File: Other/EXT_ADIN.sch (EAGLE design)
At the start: 19 parts, among them IC1 TINY45, Q1 IRLU3410, Q2 IRLU3410, Q3 IRLU3410, X2 PW1

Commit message: Added ...
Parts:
- removed IC1: TINY45, atmel:TINY15LS
- removed R1, R2, R3: 10k, RCL:R0603
- removed R4, R5, R6: 330R, RCL:R0603
- removed XS1: 1727049, Conn:1727049
- added C2, C3, C4, C5, C6: 33n, RCL:C1206
- added LED4, LED5, LED6: YELLOW, Optic:LED1206
- added Q4, Q5, Q6: BSS139, Transistor:FET-ND23
- added R1.1, R1.2: 3k3, RCL:R1206
- added R1.3, R1.4, R1.5, R1.6: 39k, RCL:R1206
- added R2.1, R2.2: 6k8, RCL:R1206
- added R2.3, R2.4, R2.5, R2.6: 10k, RCL:R1206
- added R26, R27, R28, R29, R30, R31: 470R, RCL:R1206
- added R3.1, R3.5, R3.6, R4.1, R4.2, R4.3, R4.4: n.b., RCL:R1206
- added R3.2: 560R, RCL:R1206
- added R3.3, R3.4, R4.5, R4.6: 3k6, RCL:R1206
- added XS2: 1727078, Conn:CON8-SS381
- added ZD1, ZD2, ZD3, ZD4, ZD5, ZD6: (no value), Diode:ZDSOD80
- C1: value 1u -> 33n; device RCL:C0603 -> RCL:C1206
- LED1: value LEDR -> GREEN
- LED2: value LEDG -> GREEN
- LED3: value LEDB -> YELLOW
- Q1, Q2, Q3: value IRLU3410 -> BSS139; device Transistor:FET-ND251 -> Transistor:FET-ND23
- X2: value PW1 -> (none)
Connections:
- removed net +3V3: C1.2, IC1.VCC, IN-11.S, OUT-11.S, R1.1, R2.1, R3.1
- removed net BLUE: IC1.(ADC2)PB3, Q3.G, R6.2
- removed net GREEN: IC1.(OCP)PB1, Q2.G, R5.2
- removed net N$7: Q2.D, XS1-3.K
- removed net RED: IC1.(ADC3)PB4, Q1.G, R4.2
- removed net RST: IC1.(ADC0)PB5, R1.2
- new net 3V3: IN-11.S, OUT-11.S
- new net AI6: C1.1, IN-20.S, Q1.G, R1.1.1, R2.1.1, ZD1.C
- new net AI7: C2.1, IN-19.S, Q2.G, R1.2.1, R2.2.1, ZD2.C
- new net N$10: LED2.A, R27.1
- new net N$11: Q2.S, R27.2
- new net N$12: LED3.A, R28.1
- new net N$13: Q3.S, R28.2
- new net N$14: LED4.A, R29.1
- new net N$15: Q4.S, R29.2
- new net N$16: LED5.A, R30.1
- new net N$17: Q5.S, R30.2
- new net N$18: LED6.A, R31.1
- new net N$19: Q6.S, R31.2
- new net N$2: R2.3.2, R3.3.2, R4.3.1, XS2-4.K
- new net VCC: Q1.D, Q2.D, Q3.D, Q4.D, Q5.D, Q6.D, R4.1.2, R4.2.2, R4.3.2, R4.4.2, R4.5.2, R4.6.2, X2.S, XS2-8.K
- net GND: now also C1.2, C2.2, C3.2, C4.2, C5.2, C6.2, LED4.C, LED5.C, LED6.C, R1.1.2, R1.2.2, R1.3.2, R1.4.2, R1.5.2, R1.6.2, R3.1.1, R3.2.1, R3.3.1, R3.4.1, R3.5.1, R3.6.1, XS2-3.K, ZD1.A, ZD2.A, ZD3.A, ZD4.A, ZD5.A, ZD6.A; no longer C1.1, IC1.GND, Q1.S, Q2.S, Q3.S, XS1-1.K
- net N$1: now also R2.2.2, R3.2.2, R4.2.1, XS2-2.K; no longer IN-20.S, OUT-20.S
- net N$3: now also R2.1.2, R3.1.2, R4.1.1, XS2-1.K; no longer IN-19.S, OUT-19.S
- net N$4: now also R2.4.2, R3.4.2, R4.4.1, XS2-5.K; no longer LED1.A, R4.1
- net N$5: now also R2.5.2, R3.5.2, R4.5.1, XS2-6.K; no longer LED2.A, R5.1
- net N$6: now also R2.6.2, R3.6.2, R4.6.1, XS2-7.K; no longer Q1.D, XS1-2.K
- net N$8: now also LED1.A, R26.1; no longer Q3.D, XS1-4.K
- net N$9: now also Q1.S, R26.2; no longer LED3.A, R6.1
- net PC0: now also C3.1, Q3.G, R1.3.1, R2.3.1, ZD3.C; no longer OUT-18.S
- net PC1: now also C4.1, Q4.G, R1.4.1, R2.4.1, ZD4.C; no longer OUT-17.S
- net PC2: now also C5.1, Q5.G, R1.5.1, R2.5.1, ZD5.C; no longer OUT-16.S
- net PC3: now also C6.1, Q6.G, R1.6.1, R2.6.1, ZD6.C; no longer OUT-15.S
- net PC4/SDA: no longer IC1.(AREF)PB0, R3.2
- net PC5/SCL: no longer IC1.(ADC1)PB2, R2.2
- net PD0: now also OUT-18.S; no longer OUT-10.S
- net PD1: now also OUT-17.S; no longer OUT-9.S
- net PD2: now also OUT-16.S; no longer OUT-8.S
- net PD3: now also OUT-15.S; no longer OUT-7.S
- net PD4: now also OUT-10.S; no longer OUT-6.S
- net PD5: now also OUT-9.S; no longer OUT-5.S
- net PD6: now also OUT-8.S; no longer OUT-4.S
- net PD7: now also OUT-7.S; no longer OUT-3.S
- net VIN: no longer X2.S, XS1-5.K
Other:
- note added: "0-10V"
- note added: "0-20mA"
- note added: "NPN"
- note added: "PNP"
- moved on the sheet: C1, IN-1, IN-10, IN-11, IN-12, IN-13, IN-14, IN-15, IN-16, IN-17, IN-18, IN-19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

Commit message: Reorganization
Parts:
- renumbered ZD1 to D1, ZD2 to D2, ZD3 to D3, ZD4 to D4, ZD5 to D5, ZD6 to D6

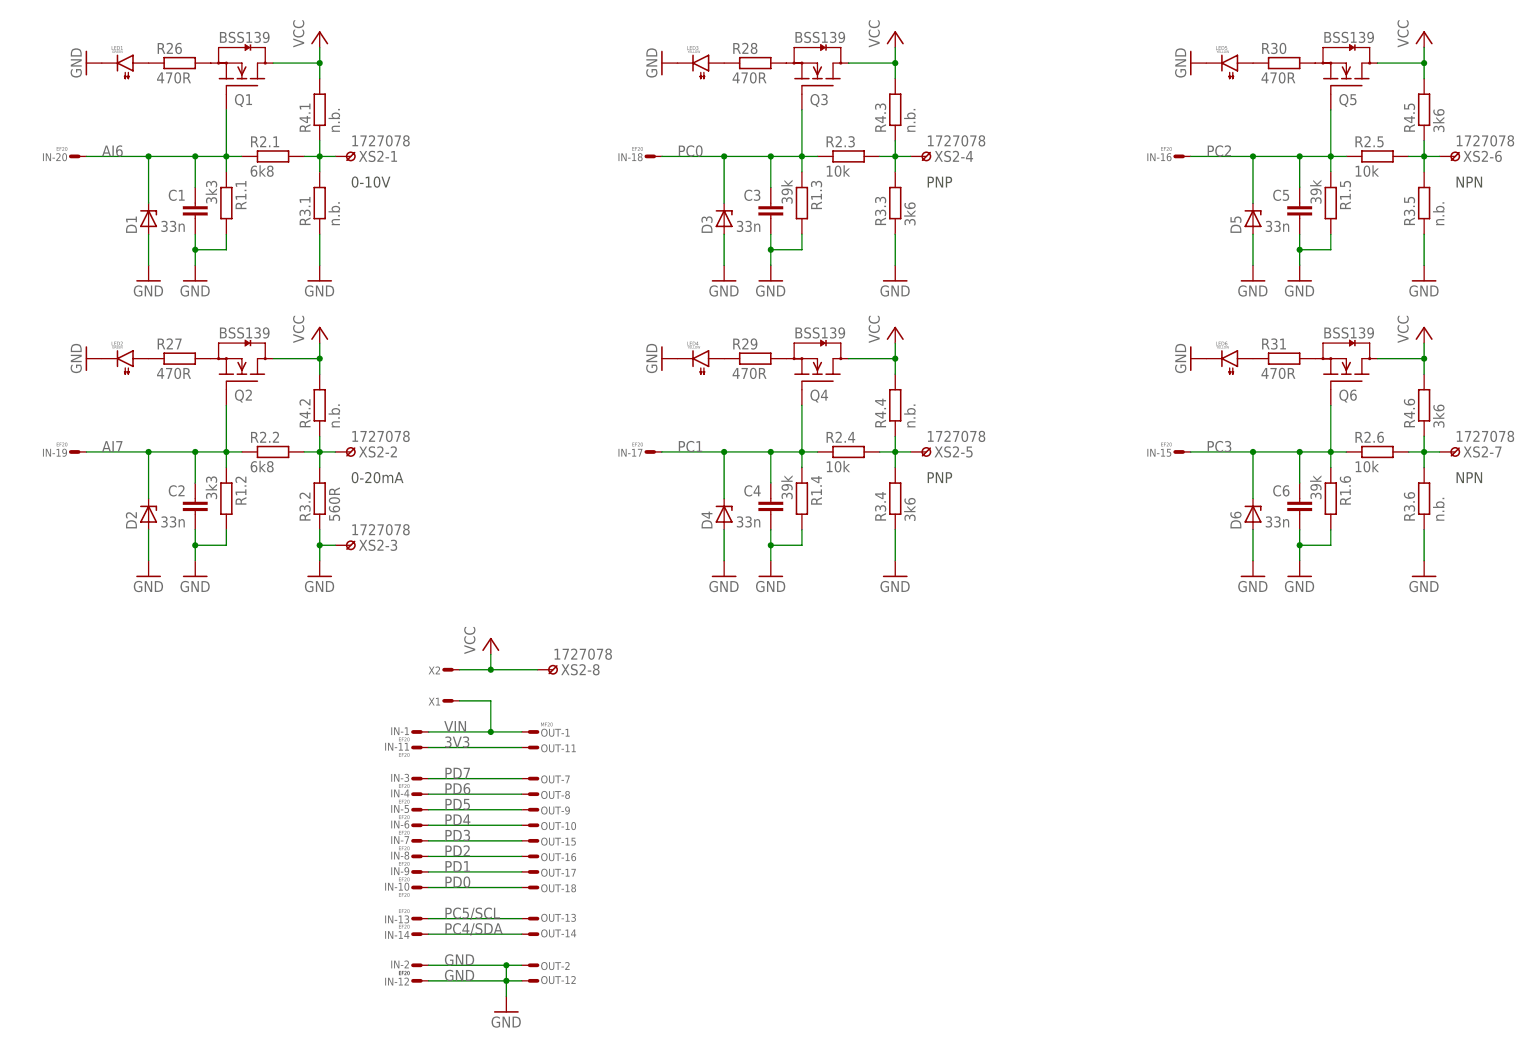
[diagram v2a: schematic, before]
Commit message: Optimized R
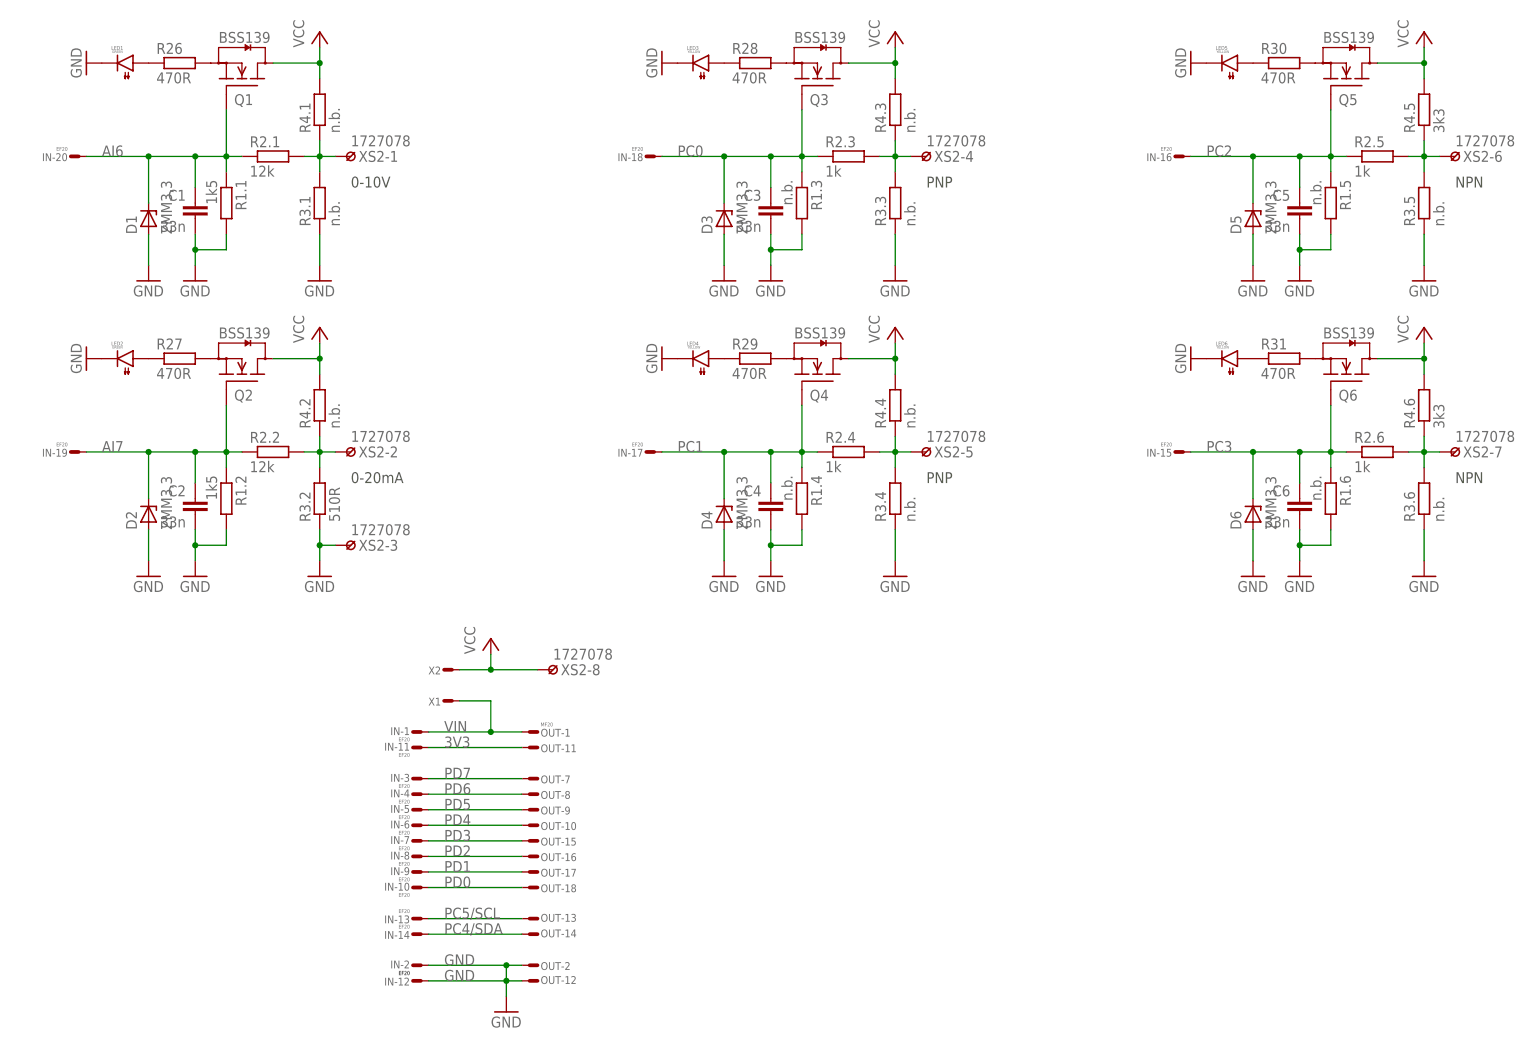
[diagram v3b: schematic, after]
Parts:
- D1, D2, D3, D4, D5, D6: value (none) -> ZMM3,3
- R1.1, R1.2: value 3k3 -> 1k5
- R1.3, R1.4, R1.5, R1.6: value 39k -> n.b.
- R2.1, R2.2: value 6k8 -> 12k
- R2.3, R2.4, R2.5, R2.6: value 10k -> 1k
- R3.2: value 560R -> 510R
- R3.3, R3.4: value 3k6 -> n.b.
- R4.5, R4.6: value 3k6 -> 3k3
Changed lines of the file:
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@@
 <part name="OUT" library="Conn" deviceset="ML20?E" device="LS" value="MF20"/>
 <part name="IN" library="Conn" deviceset="FE20E" device="LSS" value="EF20"/>
-<part name="R1.1" library="RCL" deviceset="R" device="1206" value="3k3"/>
-<part name="R2.1" library="RCL" deviceset="R" device="1206" value="6k8"/>
+<part name="R1.1" library="RCL" deviceset="R" device="1206" value="1k5"/>
+<part name="R2.1" library="RCL" deviceset="R" device="1206" value="12k"/>
 <part name="R3.1" library="RCL" deviceset="R" device="1206" value="n.b."/>
 <part name="GND1" library="supply1" deviceset="GND" device=""/>
@@
 <part name="GND2" library="supply1" deviceset="GND" device=""/>
 <part name="GND3" library="supply1" deviceset="GND" device=""/>
-<part name="D1" library="Diode" deviceset="ZD" device="SOD80"/>
+<part name="D1" library="Diode" deviceset="ZD" device="SOD80" value="ZMM3,3"/>
 <part name="GND4" library="supply1" deviceset="GND" device=""/>
 <part name="R4.1" library="RCL" deviceset="R" device="1206" value="n.b."/>
-<part name="R1.2" library="RCL" deviceset="R" device="1206" value="3k3"/>
-<part name="R2.2" library="RCL" deviceset="R" device="1206" value="6k8"/>
-<part name="R3.2" library="RCL" deviceset="R" device="1206" value="560R"/>
+<part name="R1.2" library="RCL" deviceset="R" device="1206" value="1k5"/>
+<part name="R2.2" library="RCL" deviceset="R" device="1206" value="12k"/>
+<part name="R3.2" library="RCL" deviceset="R" device="1206" value="510R"/>
 <part name="C2" library="RCL" deviceset="C" device="1206" value="33n"/>
 <part name="GND5" library="supply1" deviceset="GND" device=""/>
 <part name="GND6" library="supply1" deviceset="GND" device=""/>
-<part name="D2" library="Diode" deviceset="ZD" device="SOD80"/>
+<part name="D2" library="Diode" deviceset="ZD" device="SOD80" value="ZMM3,3"/>
 <part name="GND7" library="supply1" deviceset="GND" device=""/>
 <part name="R4.2" library="RCL" deviceset="R" device="1206" value="n.b."/>
 <part name="P+1" library="supply1" deviceset="VCC" device=""/>
 <part name="P+2" library="supply1" deviceset="VCC" device=""/>
-<part name="R1.3" library="RCL" deviceset="R" device="1206" value="39k"/>
-<part name="R2.3" library="RCL" deviceset="R" device="1206" value="10k"/>
-<part name="R3.3" library="RCL" deviceset="R" device="1206" value="3k6"/>
+<part name="R1.3" library="RCL" deviceset="R" device="1206" value="n.b."/>
+<part name="R2.3" library="RCL" deviceset="R" device="1206" value="1k"/>
+<part name="R3.3" library="RCL" deviceset="R" device="1206" value="n.b."/>
 <part name="C3" library="RCL" deviceset="C" device="1206" value="33n"/>
 <part name="GND8" library="supply1" deviceset="GND" device=""/>
 <part name="GND9" library="supply1" deviceset="GND" device=""/>
-<part name="D3" library="Diode" deviceset="ZD" device="SOD80"/>
+<part name="D3" library="Diode" deviceset="ZD" device="SOD80" value="ZMM3,3"/>
 <part name="GND10" library="supply1" deviceset="GND" device=""/>
 <part name="R4.3" library="RCL" deviceset="R" device="1206" value="n.b."/>
-<part name="R1.4" library="RCL" deviceset="R" device="1206" value="39k"/>
-<part name="R2.4" library="RCL" deviceset="R" device="1206" value="10k"/>
-<part name="R3.4" library="RCL" deviceset="R" device="1206" value="3k6"/>
+<part name="R1.4" library="RCL" deviceset="R" device="1206" value="n.b."/>
+<part name="R2.4" library="RCL" deviceset="R" device="1206" value="1k"/>
+<part name="R3.4" library="RCL" deviceset="R" device="1206" value="n.b."/>
 <part name="C4" library="RCL" deviceset="C" device="1206" value="33n"/>
 <part name="GND11" library="supply1" deviceset="GND" device=""/>
 <part name="GND12" library="supply1" deviceset="GND" device=""/>
-<part name="D4" library="Diode" deviceset="ZD" device="SOD80"/>
+<part name="D4" library="Diode" deviceset="ZD" device="SOD80" value="ZMM3,3"/>
 <part name="GND13" library="supply1" deviceset="GND" device=""/>
 <part name="R4.4" library="RCL" deviceset="R" device="1206" value="n.b."/>
 <part name="P+3" library="supply1" deviceset="VCC" device=""/>
 <part name="P+4" library="supply1" deviceset="VCC" device=""/>
-<part name="R1.5" library="RCL" deviceset="R" device="1206" value="39k"/>
-<part name="R2.5" library="RCL" deviceset="R" device="1206" value="10k"/>
+<part name="R1.5" library="RCL" deviceset="R" device="1206" value="n.b."/>
+<part name="R2.5" library="RCL" deviceset="R" device="1206" value="1k"/>
 <part name="R3.5" library="RCL" deviceset="R" device="1206" value="n.b."/>
 <part name="C5" library="RCL" deviceset="C" device="1206" value="33n"/>
 <part name="GND14" library="supply1" deviceset="GND" device=""/>
 <part name="GND15" library="supply1" deviceset="GND" device=""/>
-<part name="D5" library="Diode" deviceset="ZD" device="SOD80"/>
+<part name="D5" library="Diode" deviceset="ZD" device="SOD80" value="ZMM3,3"/>
 <part name="GND16" library="supply1" deviceset="GND" device=""/>
-<part name="R4.5" library="RCL" deviceset="R" device="1206" value="3k6"/>
-<part name="R1.6" library="RCL" deviceset="R" device="1206" value="39k"/>
-<part name="R2.6" library="RCL" deviceset="R" device="1206" value="10k"/>
+<part name="R4.5" library="RCL" deviceset="R" device="1206" value="3k3"/>
+<part name="R1.6" library="RCL" deviceset="R" device="1206" value="n.b."/>
+<part name="R2.6" library="RCL" deviceset="R" device="1206" value="1k"/>
 <part name="R3.6" library="RCL" deviceset="R" device="1206" value="n.b."/>
 <part name="C6" library="RCL" deviceset="C" device="1206" value="33n"/>
 <part name="GND17" library="supply1" deviceset="GND" device=""/>
 <part name="GND18" library="supply1" deviceset="GND" device=""/>
-<part name="D6" library="Diode" deviceset="ZD" device="SOD80"/>
+<part name="D6" library="Diode" deviceset="ZD" device="SOD80" value="ZMM3,3"/>
 <part name="GND19" library="supply1" deviceset="GND" device=""/>
-<part name="R4.6" library="RCL" deviceset="R" device="1206" value="3k6"/>
+<part name="R4.6" library="RCL" deviceset="R" device="1206" value="3k3"/>
 <part name="P+5" library="supply1" deviceset="VCC" device=""/>
 <part name="P+6" library="supply1" deviceset="VCC" device=""/>

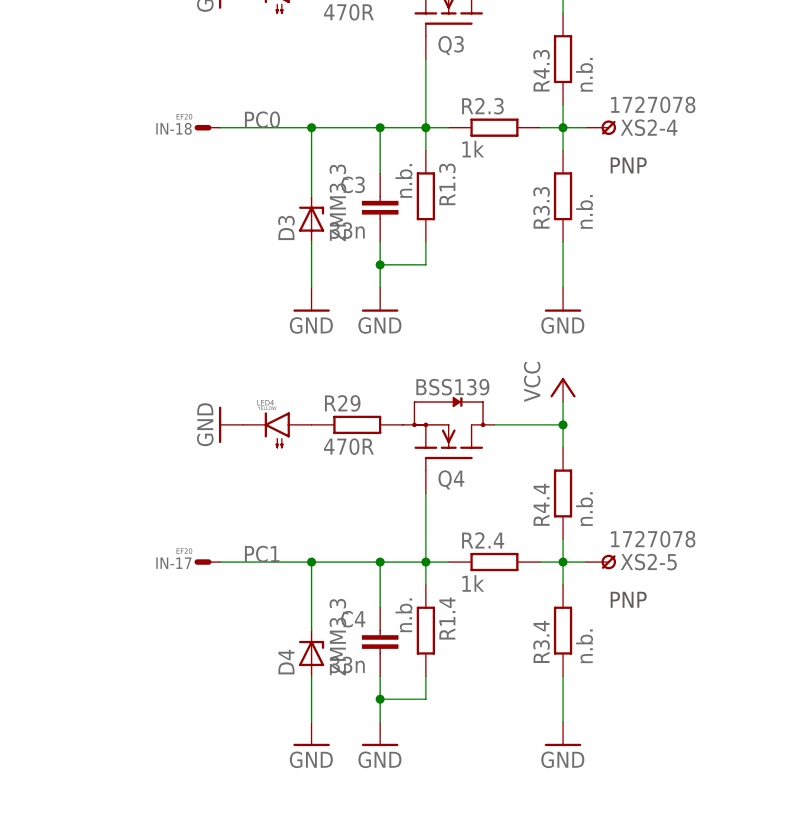
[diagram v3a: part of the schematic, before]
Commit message: Added AC Dimmer
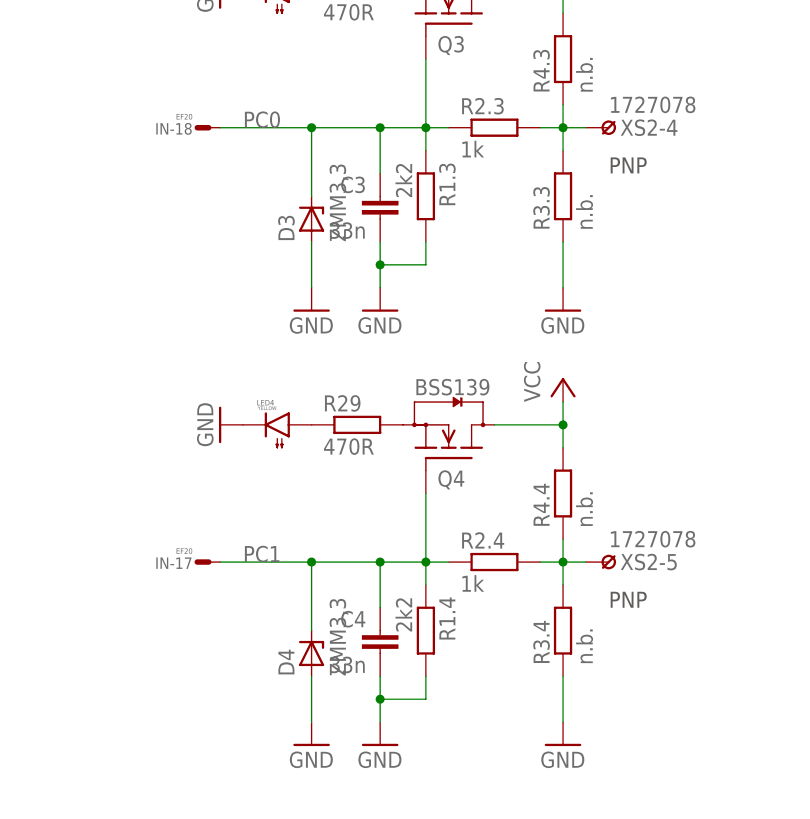
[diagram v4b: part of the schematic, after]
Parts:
- R1.3, R1.4: value n.b. -> 2k2
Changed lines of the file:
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@@
 <part name="P+1" library="supply1" deviceset="VCC" device=""/>
 <part name="P+2" library="supply1" deviceset="VCC" device=""/>
-<part name="R1.3" library="RCL" deviceset="R" device="1206" value="n.b."/>
+<part name="R1.3" library="RCL" deviceset="R" device="1206" value="2k2"/>
 <part name="R2.3" library="RCL" deviceset="R" device="1206" value="1k"/>
 <part name="R3.3" library="RCL" deviceset="R" device="1206" value="n.b."/>
@@
 <part name="GND10" library="supply1" deviceset="GND" device=""/>
 <part name="R4.3" library="RCL" deviceset="R" device="1206" value="n.b."/>
-<part name="R1.4" library="RCL" deviceset="R" device="1206" value="n.b."/>
+<part name="R1.4" library="RCL" deviceset="R" device="1206" value="2k2"/>
 <part name="R2.4" library="RCL" deviceset="R" device="1206" value="1k"/>
 <part name="R3.4" library="RCL" deviceset="R" device="1206" value="n.b."/>
